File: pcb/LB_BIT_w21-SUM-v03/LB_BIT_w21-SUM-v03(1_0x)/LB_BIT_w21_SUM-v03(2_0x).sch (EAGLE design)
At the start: 23 parts

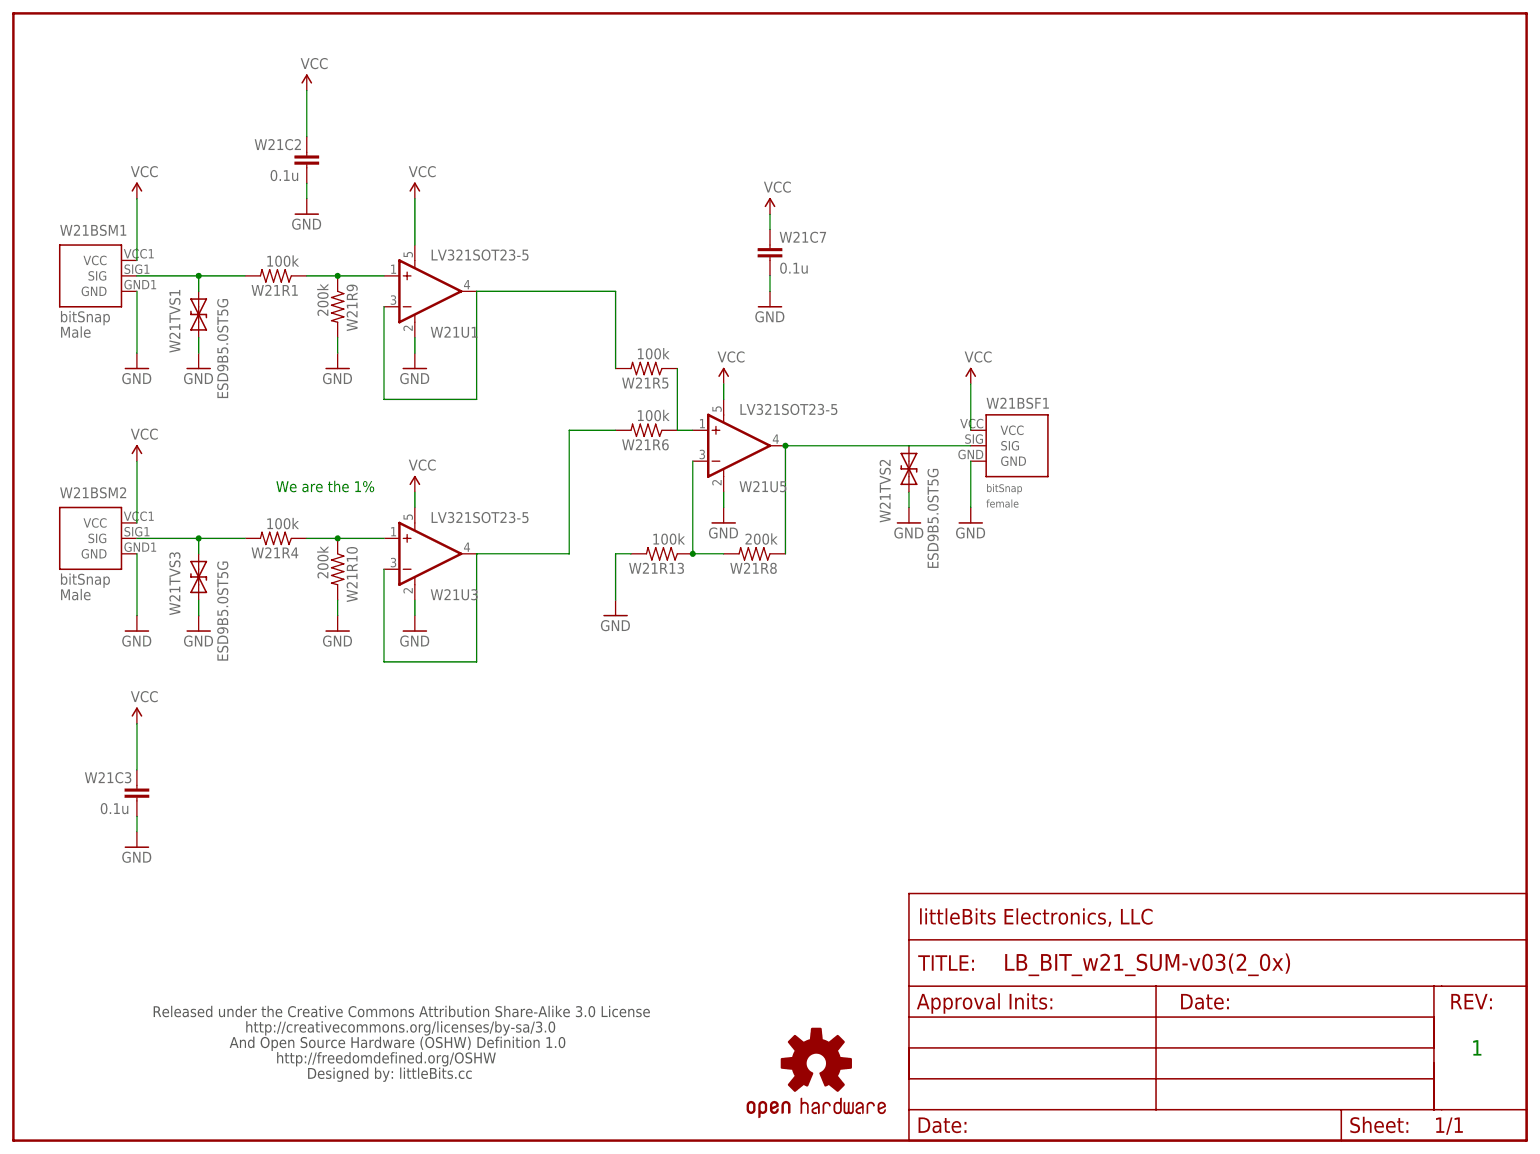
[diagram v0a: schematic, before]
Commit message: Second revision of schematic, and created simulation and PCB file
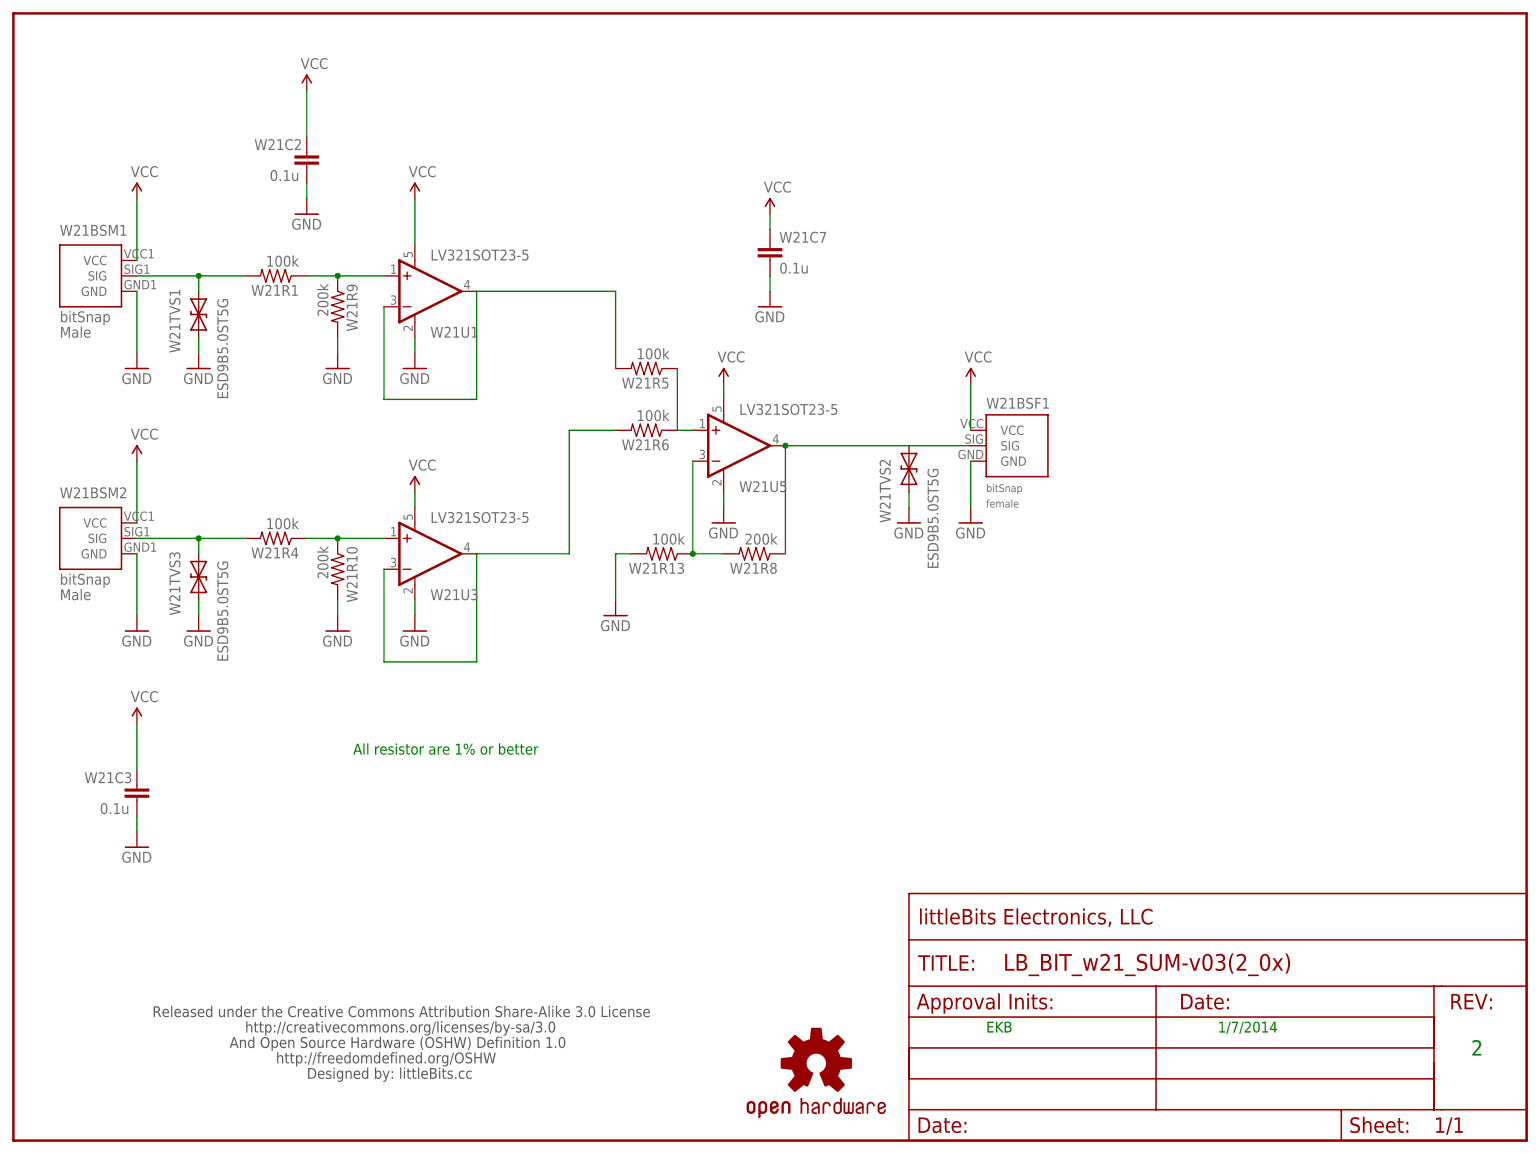
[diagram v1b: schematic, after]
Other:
- note added: "1/7/2014"
- note added: "2"
- note added: "All resistor are 1% or better"
- note added: "EKB"
- note removed: "1"
- note removed: "We are the 1%"
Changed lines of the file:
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@@
 <sheet>
 <plain>
-<text x="239.776" y="13.97" size="2.54" layer="91">1</text>
-<text x="43.18" y="106.68" size="1.778" layer="91">We are the 1%</text>
+<text x="239.776" y="13.97" size="2.54" layer="91">2</text>
+<text x="55.88" y="63.5" size="1.778" layer="91">All resistor are 1% or better</text>
+<text x="160.02" y="17.78" size="1.778" layer="91">EKB</text>
+<text x="198.12" y="17.78" size="1.778" layer="91">1/7/2014</text>
 </plain>
 <instances>
